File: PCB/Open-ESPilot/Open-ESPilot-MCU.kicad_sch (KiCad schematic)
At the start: 15 parts, among them J1 USB_C_Receptacle_USB2.0_16P, SW1 SW_Push, SW2 SW_Push, U1 ESP32-S3-WROOM-1-N8

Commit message: Assigned footprints and components for the easy ones (R,C,JP,J)
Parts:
- C2, C3, C4, C5: footprint (none) -> Capacitor_SMD:C_0805_2012Metric_Pad1.18x1.45mm_HandSolder
- J1: LCSC (none) -> C165948
- R1, R2, R3, R4: footprint (none) -> Resistor_SMD:R_0805_2012Metric_Pad1.20x1.40mm_HandSolder
- SW1, SW2: footprint (none) -> Button_Switch_SMD:SW_Push_SPST_NO_Alps_SKRK; LCSC (none) -> C115357
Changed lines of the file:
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@@
 			)
 		)
-		(property "Footprint" ""
+		(property "Footprint" "Resistor_SMD:R_0805_2012Metric_Pad1.20x1.40mm_HandSolder"
 			(at 198.882 76.2 90)
 			(effects
@@
 			)
 		)
-		(property "Footprint" ""
+		(property "Footprint" "Capacitor_SMD:C_0805_2012Metric_Pad1.18x1.45mm_HandSolder"
 			(at 248.6152 142.24 0)
 			(effects
@@
 			)
 		)
-		(property "Footprint" ""
+		(property "Footprint" "Capacitor_SMD:C_0805_2012Metric_Pad1.18x1.45mm_HandSolder"
 			(at 47.9552 44.45 0)
 			(effects
@@
 			)
 		)
-		(property "Footprint" ""
+		(property "Footprint" "Capacitor_SMD:C_0805_2012Metric_Pad1.18x1.45mm_HandSolder"
 			(at 101.2952 43.18 0)
 			(effects
@@
 			)
 		)
-		(property "Footprint" ""
+		(property "Footprint" "Resistor_SMD:R_0805_2012Metric_Pad1.20x1.40mm_HandSolder"
 			(at 206.502 76.2 90)
 			(effects
@@
 			)
 		)
-		(property "Footprint" ""
+		(property "Footprint" "Button_Switch_SMD:SW_Push_SPST_NO_Alps_SKRK"
 			(at 203.2 138.43 0)
 			(effects
@@
 		(property "Description" "Push button switch, generic, two pins"
 			(at 208.28 138.43 0)
+			(effects
+				(font
+					(size 1.27 1.27)
+				)
+				(hide yes)
+			)
+		)
+		(property "LCSC" "C115357"
+			(at 208.28 138.43 90)
 			(effects
 				(font
@@
 			)
 		)
-		(property "Footprint" ""
+		(property "Footprint" "Resistor_SMD:R_0805_2012Metric_Pad1.20x1.40mm_HandSolder"
 			(at 253.492 124.46 90)
 			(effects
@@
 			)
 		)
-		(property "Footprint" ""
+		(property "Footprint" "Capacitor_SMD:C_0805_2012Metric_Pad1.18x1.45mm_HandSolder"
 			(at 201.6252 142.24 0)
 			(effects
@@
 			)
 		)
-		(property "Footprint" ""
+		(property "Footprint" "Resistor_SMD:R_0805_2012Metric_Pad1.20x1.40mm_HandSolder"
 			(at 206.502 124.46 90)
 			(effects
@@
 			)
 		)
-		(property "Footprint" ""
+		(property "Footprint" "Button_Switch_SMD:SW_Push_SPST_NO_Alps_SKRK"
 			(at 250.19 138.43 0)
 			(effects
@@
 			)
 		)
+		(property "LCSC" "C115357"
+			(at 255.27 138.43 90)
+			(effects
+				(font
+					(size 1.27 1.27)
+				)
+				(hide yes)
+			)
+		)
 		(pin "2"
 		)
@@
 			(at 238.76 52.07 0)
 			(effects
+				(font
+					(size 1.27 1.27)
+				)
+				(hide yes)
+			)
+		)
+		(property "LCSC" "C165948"
+			(at 238.76 52.07 0)
+			(effects

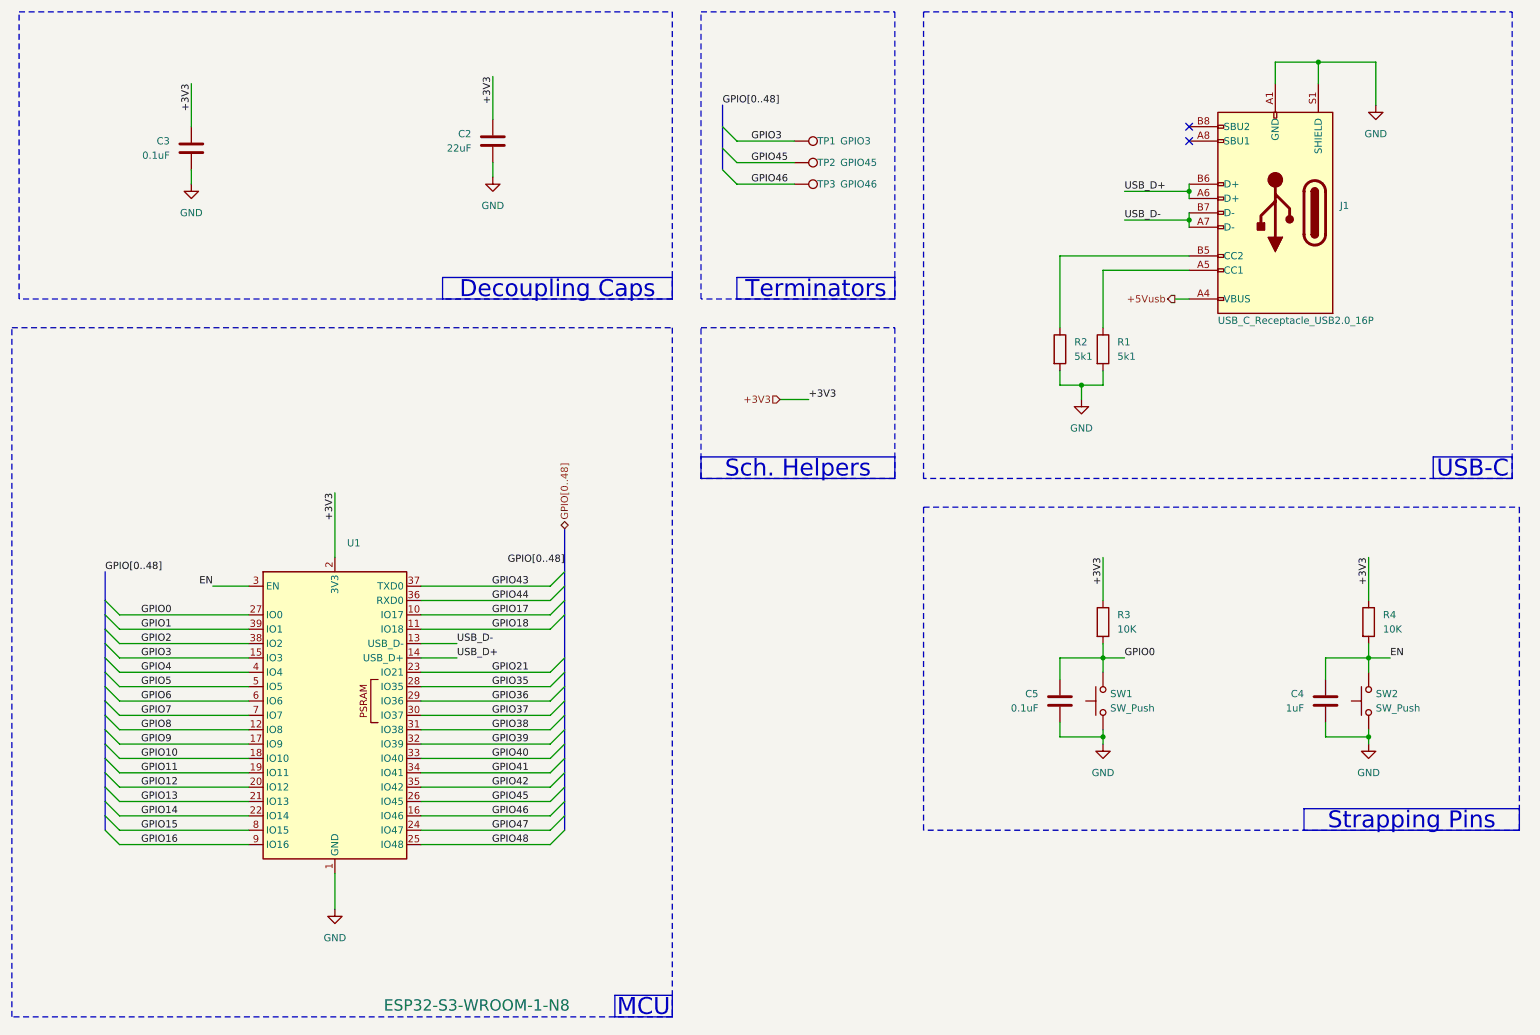
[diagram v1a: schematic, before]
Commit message: rearenged pins and moved polyfuse.
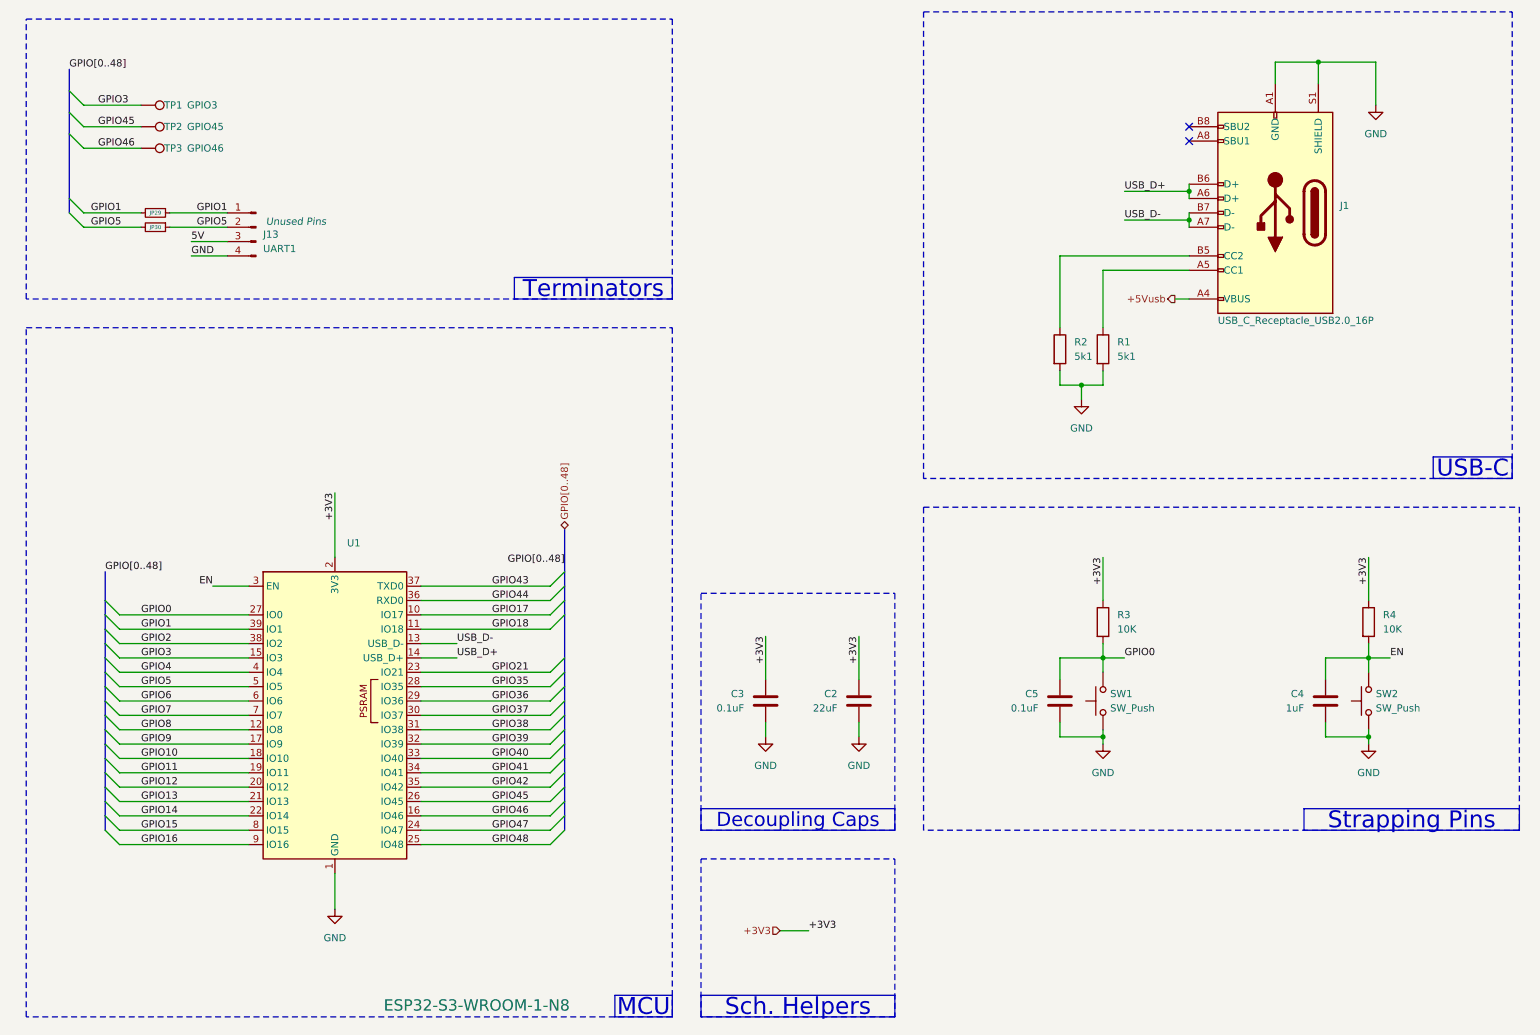
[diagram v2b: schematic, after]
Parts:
- added J13: UART1, Connector_PinHeader_2.54mm:PinHeader_1x04_P2.54mm_Vertical, symbol Connector:Conn_01x04_Pin
- added JP29, JP30: R_Small, Jumper:SolderJumper-2_P1.3mm_Bridged2Bar_RoundedPad1.0x1.5mm, symbol Device:R_Small
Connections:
- net GND: now also J13.4 (Pin_4)
- net GPIO1: now also J13.1 (Pin_1), JP29.1, JP29.2
- net GPIO5: now also J13.2 (Pin_2), JP30.1, JP30.2
- new net 5V: J13.3 (Pin_3)
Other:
- moved on the sheet: C2, C3, TP1, TP2, TP3

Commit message: Added new footprints for power pads and added decoupling capacitors.
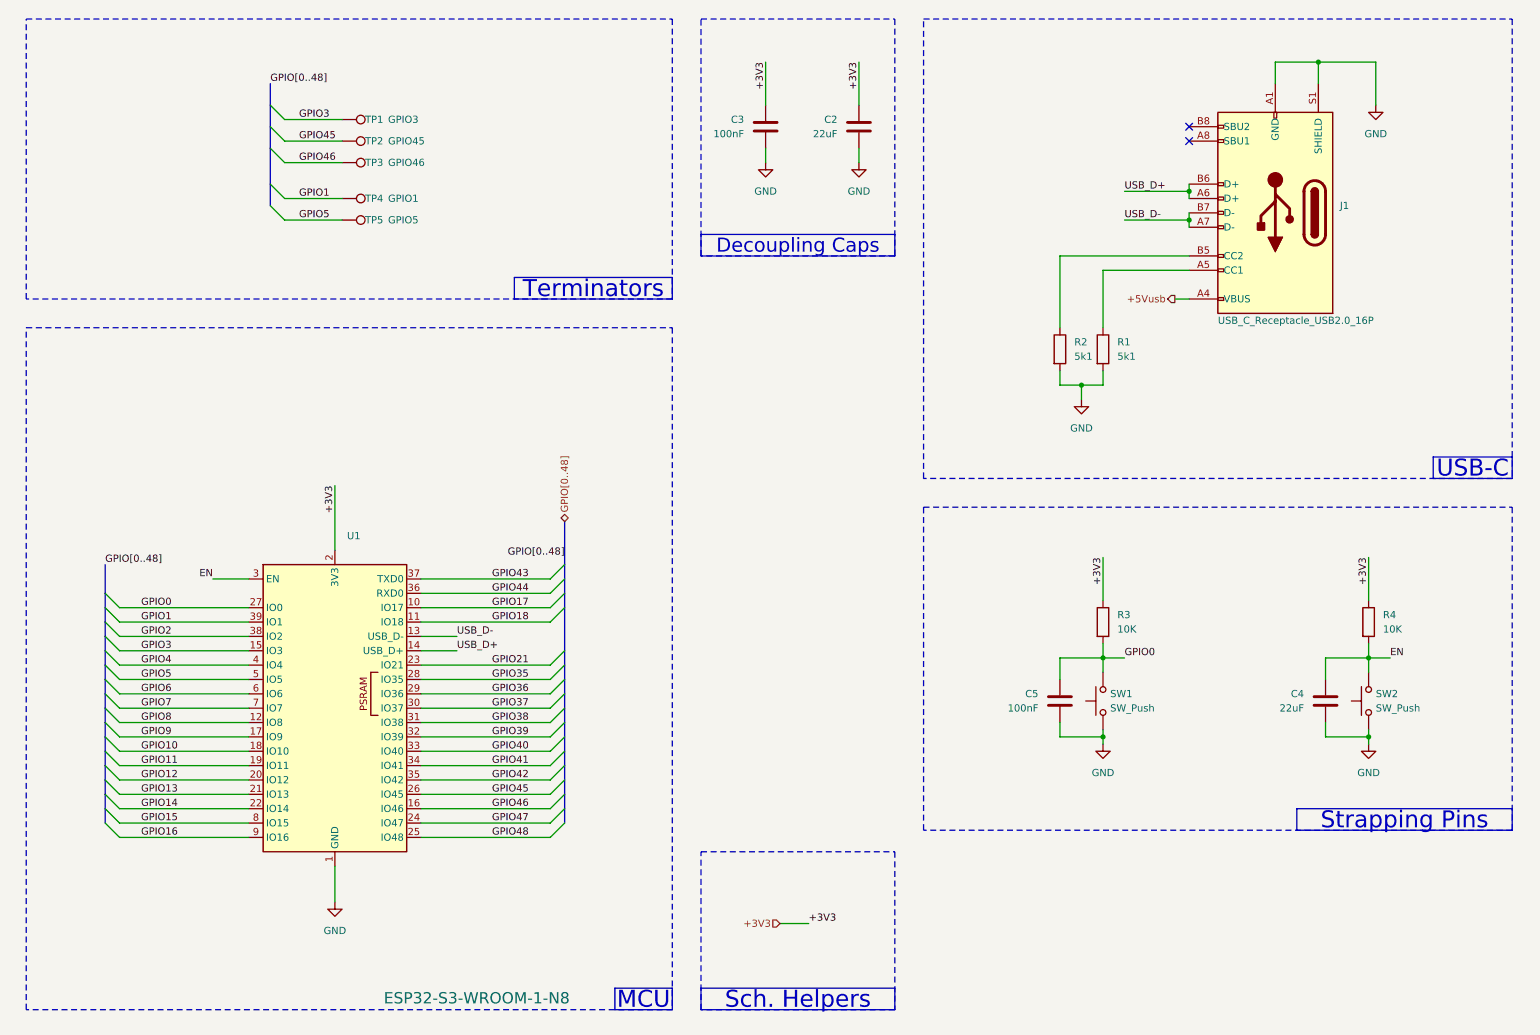
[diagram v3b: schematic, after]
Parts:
- removed J13: UART1, Connector_PinHeader_2.54mm:PinHeader_1x04_P2.54mm_Vertical, symbol Connector:Conn_01x04_Pin
- removed JP29, JP30: R_Small, Jumper:SolderJumper-2_P1.3mm_Bridged2Bar_RoundedPad1.0x1.5mm, symbol Device:R_Small
- added TP4: GPIO1, TestPoint:TestPoint_THTPad_D2.0mm_Drill1.0mm, symbol Connector:TestPoint
- added TP5: GPIO5, TestPoint:TestPoint_THTPad_D2.0mm_Drill1.0mm, symbol Connector:TestPoint
- C2: Function (none) -> Decoupling; LCSC (none) -> C5674
- C3: value 0.1uF -> 100nF; Function (none) -> Decoupling
- C4: value 1uF -> 22uF
- C5: value 0.1uF -> 100nF
- TP1, TP2, TP3: footprint (none) -> TestPoint:TestPoint_THTPad_D2.0mm_Drill1.0mm
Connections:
- net GPIO1: now also TP4.1
- net GPIO5: now also TP5.1
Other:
- moved on the sheet: C2, C3, TP1, TP2, TP3, U1

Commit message: Added Ferite bead for the ESP.
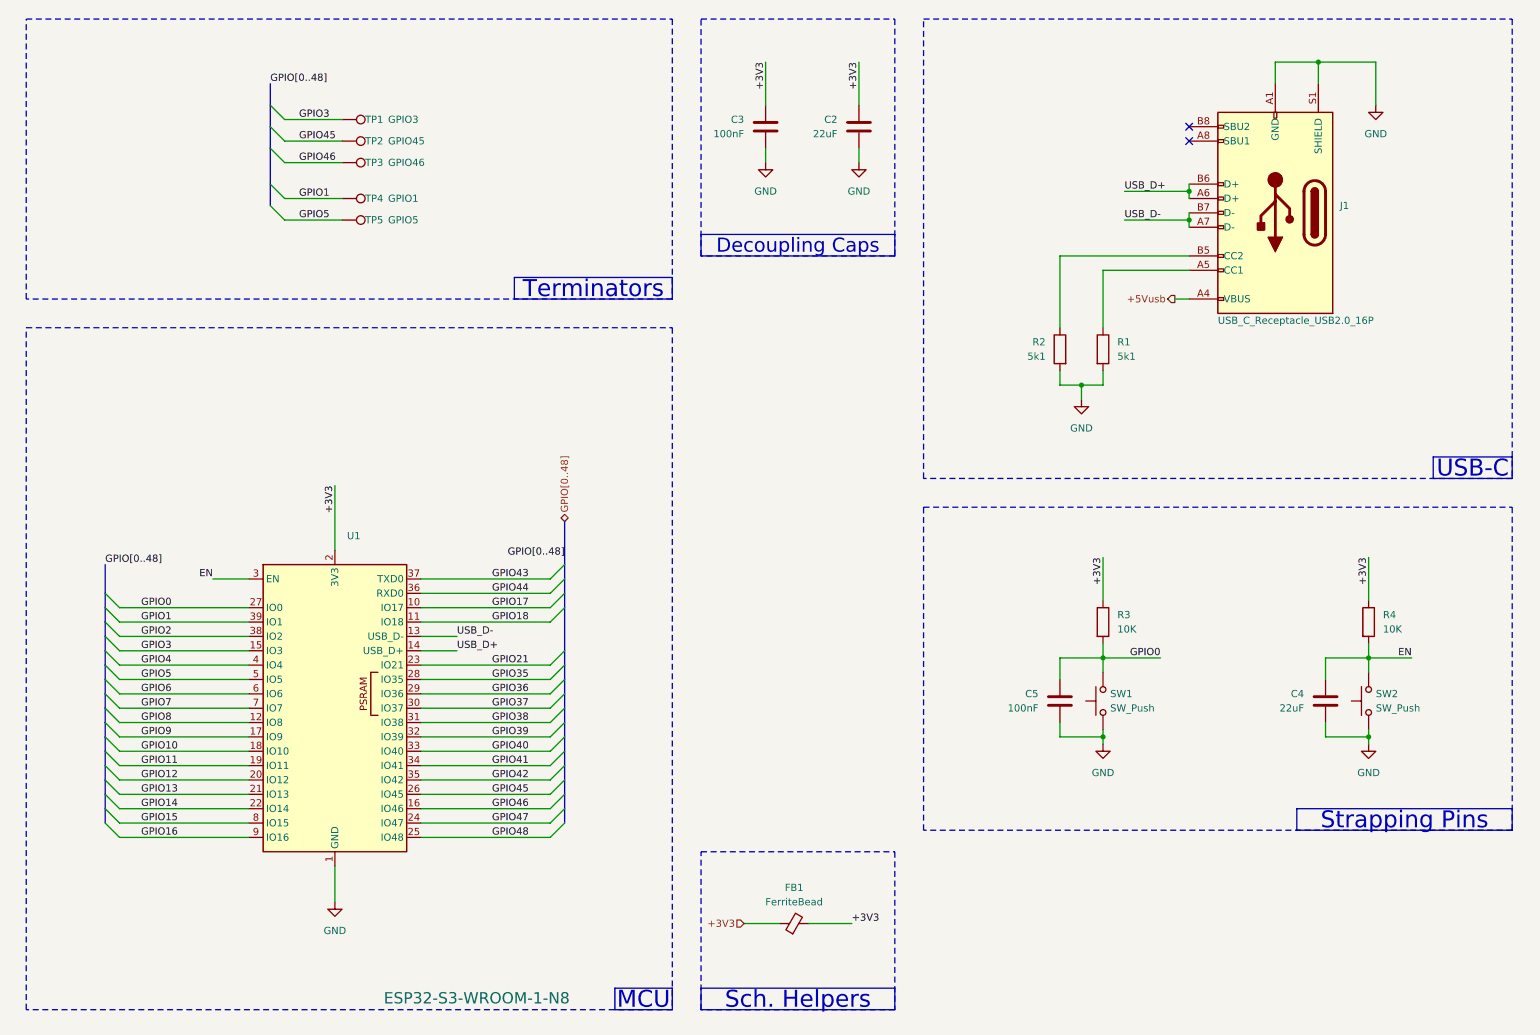
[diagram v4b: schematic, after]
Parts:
- added FB1: FerriteBead, Inductor_SMD:L_0805_2012Metric_Pad1.05x1.20mm_HandSolder, symbol Device:FerriteBead_Small
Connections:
- net +3V3: now also FB1.1, FB1.2
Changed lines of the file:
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@@
 	(wire
 		(pts
-			(xy 255.27 130.81) (xy 259.08 130.81)
-		)
-		(stroke
-			(width 0)
-			(type default)
-		)
-	)
-	(wire
-		(pts
 			(xy 110.49 157.48) (xy 87.63 157.48)
 		)
@@
 	(wire
 		(pts
+			(xy 218.44 130.81) (xy 208.28 130.81)
+		)
+		(stroke
+			(width 0)
+			(type default)
+		)
+	)
+	(wire
+		(pts
 			(xy 63.5 43.18) (xy 73.66 43.18)
 		)
@@
 		)
 	)
-	(wire
-		(pts
-			(xy 208.28 130.81) (xy 212.09 130.81)
-		)
-		(stroke
-			(width 0)
-			(type default)
-		)
-	)
 	(bus
 		(pts
@@
 	(wire
 		(pts
-			(xy 151.13 177.8) (xy 156.21 177.8)
+			(xy 144.78 177.8) (xy 151.13 177.8)
+		)
+		(stroke
+			(width 0)
+			(type default)
+		)
+	)
+	(wire
+		(pts
+			(xy 156.21 177.8) (xy 163.83 177.8)
 		)
 		(stroke
@@
 	(wire
 		(pts
+			(xy 262.89 130.81) (xy 255.27 130.81)
+		)
+		(stroke
+			(width 0)
+			(type default)
+		)
+	)
+	(wire
+		(pts
 			(xy 255.27 144.78) (xy 255.27 143.51)
 		)
@@
 	)
 	(label "GPIO0"
-		(at 212.09 130.81 0)
+		(at 218.44 130.81 180)
 		(effects
 			(font
 				(size 1.27 1.27)
 			)
-			(justify left bottom)
+			(justify right bottom)
 		)
 	)
@@
 	)
 	(label "+3V3"
-		(at 156.21 177.8 0)
+		(at 163.83 177.8 0)
 		(effects
 			(font
@@
 	)
 	(label "EN"
-		(at 259.08 130.81 0)
+		(at 262.89 130.81 180)
 		(effects
 			(font
 				(size 1.27 1.27)
 			)
-			(justify left bottom)
+			(justify right bottom)
 		)
 	)
@@
 	(hierarchical_label "+3V3"
 		(shape input)
-		(at 151.13 177.8 180)
+		(at 144.78 177.8 180)
 		(effects
 			(font
@@
 		(lib_id "Device:R")
 		(at 200.66 76.2 0)
+		(mirror y)
 		(unit 1)
 		(exclude_from_sim no)
@@
 		(on_board yes)
 		(dnp no)
-		(fields_autoplaced yes)
 		(property "Reference" "R2"
-			(at 203.2 74.9299 0)
+			(at 198.12 74.9299 0)
 			(effects
 				(font
@@
 		)
 		(property "Value" "5k1"
-			(at 203.2 77.4699 0)
+			(at 198.12 77.4699 0)
 			(effects
 				(font
@@
 		)
 		(property "Footprint" "Resistor_SMD:R_0805_2012Metric_Pad1.20x1.40mm_HandSolder"
-			(at 198.882 76.2 90)
+			(at 202.438 76.2 90)
 			(effects
 				(font
@@
 					(unit 1)
 				)
+			)
+		)
+	)
+	(symbol
+		(lib_id "Device:FerriteBead_Small")
+		(at 153.67 177.8 90)
+		(unit 1)
+		(exclude_from_sim no)
+		(in_bom yes)
+		(on_board yes)
+		(dnp no)
+		(fields_autoplaced yes)
+		(property "Reference" "FB1"
+			(at 153.6319 171.45 90)
+			(effects
+				(font
+					(size 1.27 1.27)
+				)
+			)
+		)
+		(property "Value" "FerriteBead"
+			(at 153.6319 173.99 90)
+			(effects
+				(font
+					(size 1.27 1.27)
+				)
+			)
+		)
+		(property "Footprint" "Inductor_SMD:L_0805_2012Metric_Pad1.05x1.20mm_HandSolder"
+			(at 153.67 179.578 90)
+			(effects
+				(font
+					(size 1.27 1.27)
+				)
+				(hide yes)
+			)
+		)
+		(property "Datasheet" "~"
+			(at 153.67 177.8 0)
+			(effects
+				(font
+					(size 1.27 1.27)
+				)
+				(hide yes)
+			)
+		)
+		(property "Description" "Ferrite bead, small symbol"
+			(at 153.67 177.8 0)
+			(effects
+				(font
+					(size 1.27 1.27)
+				)
+				(hide yes)
+			)
+		)
+		(property "LCSC" "C15957"
+			(at 153.67 177.8 90)
+			(effects
+				(font
+					(size 1.27 1.27)
+				)
+				(hide yes)
+			)
+		)
+		(pin "1"
+		)
+		(pin "2"
+		)
+		(instances
+			(project ""
+				(path "/2992e60d-a645-4cd7-90ae-fe72311b6bee/83c0ee2d-1731-42ff-aa2e-45ac54ea980d"
+					(reference "FB1")
+					(unit 1)
+				)
